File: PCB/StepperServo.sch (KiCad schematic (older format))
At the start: 69 parts, among them P1 Conn_01x06, P2 Conn_01x04, P4 Conn_01x08, P5 Conn_01x02, U1 BNOR11, U2 A4950E, U4 A4950E, U5 TLE5012B, U7 STM32F103CBTx, U8 LD1117S33CTR, U9 PCA82C251, Y1 Crystal, p7 Conn_01x08

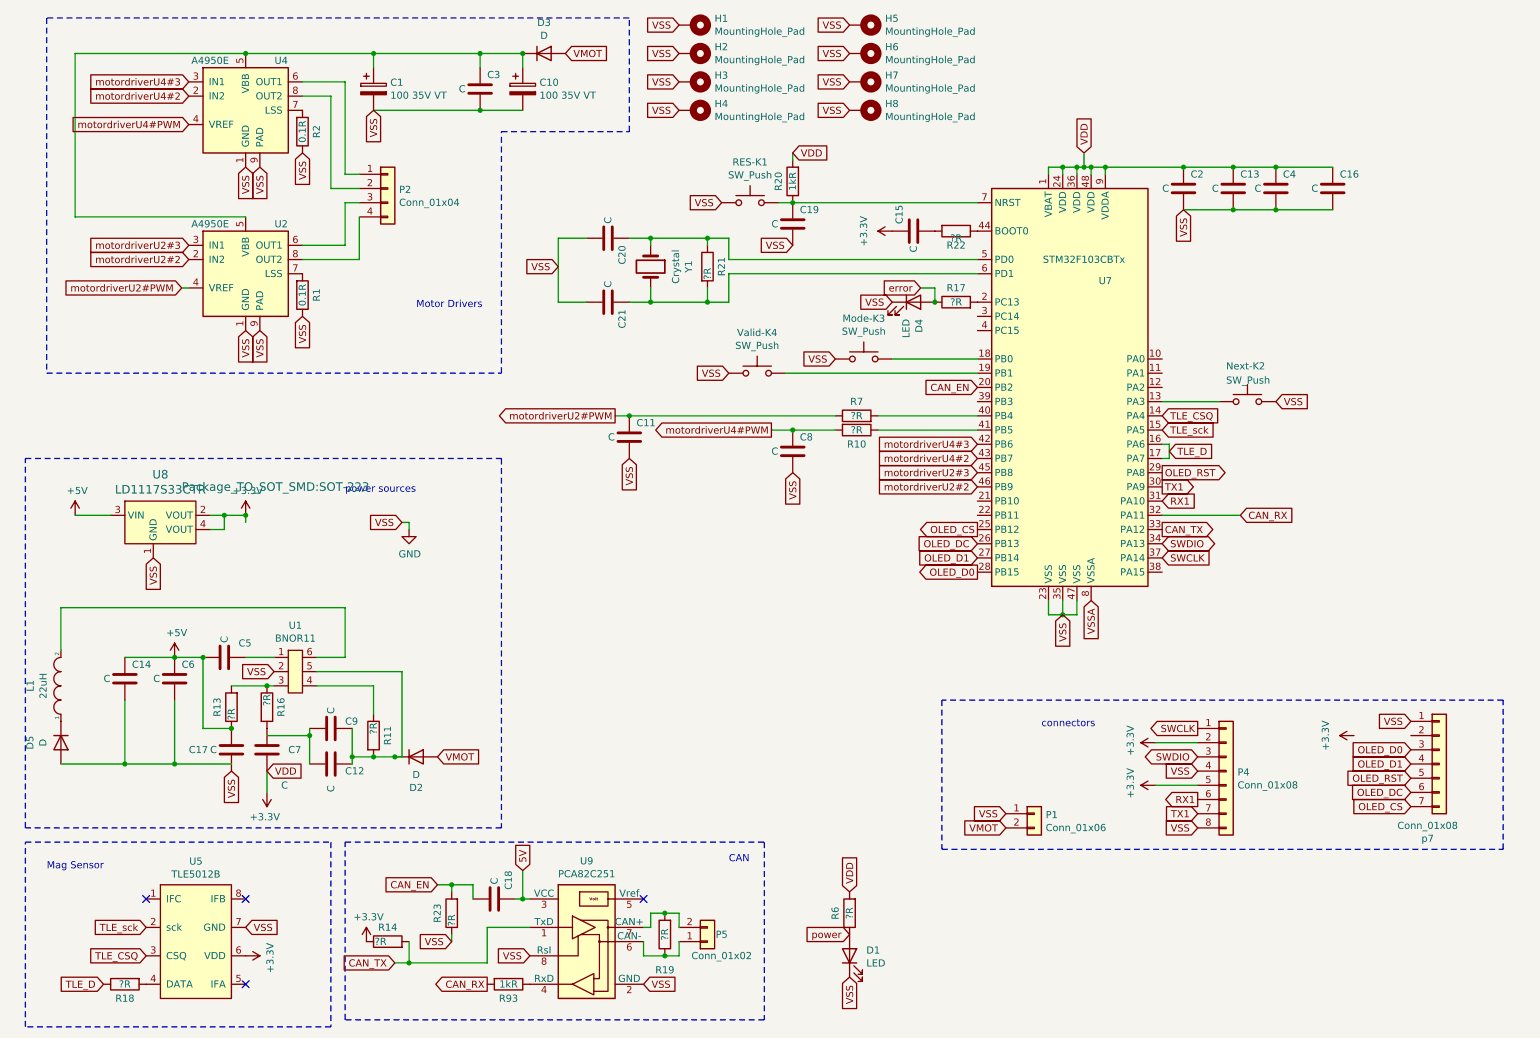
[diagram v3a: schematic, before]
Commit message: Boot0 to gnd
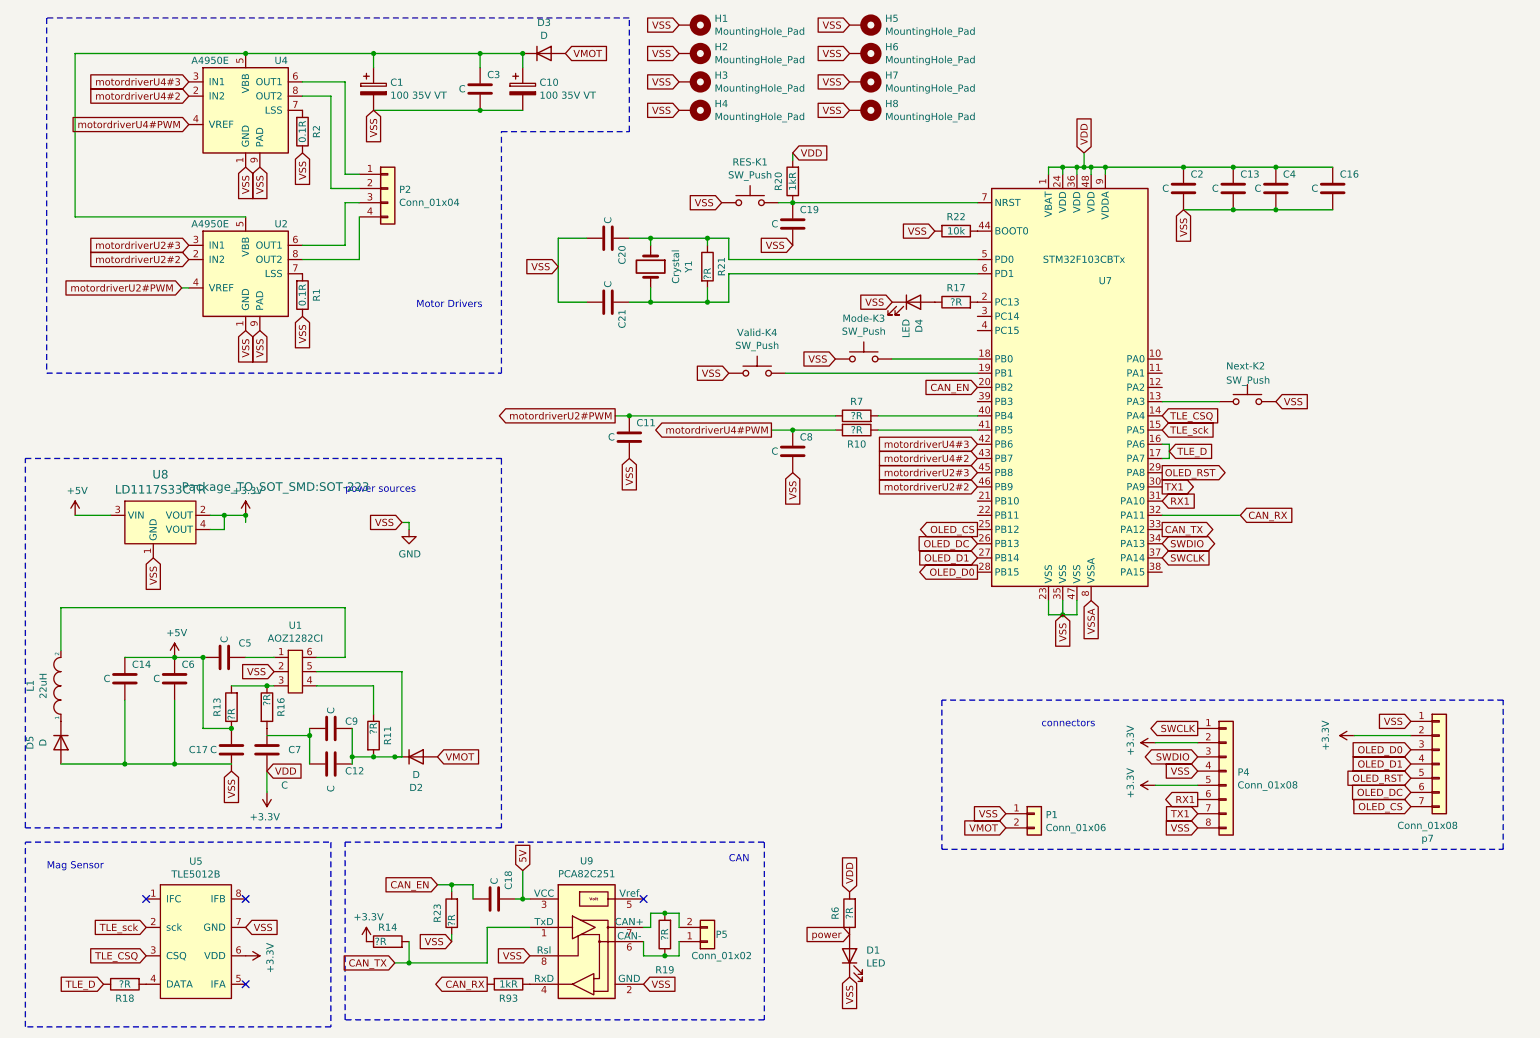
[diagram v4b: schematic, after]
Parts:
- removed C15: C, Capacitor_SMD:C_0603_1608Metric, symbol StepperServo-rescue:C-Device-BTTS57Bv2-rescue
- R22: value ?R -> 10k
- U1: value BNOR11 -> AOZ1282CI
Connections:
- net +3V3: now also p7.2 (Pin_2)
- net GND: now also R22.2
- net error: no longer names the net of D4.2 (A), R17.1
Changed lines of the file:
@@
-$EndComp
-$Comp
-L StepperServo-rescue:R-Device-BTTS57Bv2-rescue R17
-U 1 1 60AF1C31
-P 7150 2600
-F 0 "R17" V 7250 2600 50  0000 C CNN
-F 1 "?R" V 7150 2600 50  0000 C CNN
-F 2 "Resistor_SMD:R_0603_1608Metric" V 7080 2600 50  0001 C CNN
-F 3 "~" H 7150 2600 50  0001 C CNN
-	1    7150 2600
-	0    -1   -1   0
 $EndComp
 $Comp
@@
 Text GLabel 6400 7050 0    50   Input ~ 0
 power
-Text GLabel 6900 2500 0    50   Input ~ 0
-error
 Text GLabel 6700 2600 0    50   Input ~ 0
 VSS
@@
 	1    0    0    -1
 $EndComp
-Wire Wire Line
-	6900 2500 7000 2500
-Wire Wire Line
-	7000 2500 7000 2600
-Connection ~ 7000 2600
 $Comp
 L TLE5012B:TLE5012B U5
@@
 $EndComp
 $Comp
-L StepperServo-rescue:C-Device-BTTS57Bv2-rescue C15
-U 1 1 60B85066
-P 6850 2100
-F 0 "C15" H 6900 2200 50  0000 L CNN
-F 1 "C" H 6700 2100 50  0000 L CNN
-F 2 "Capacitor_SMD:C_0603_1608Metric" H 6888 1950 50  0001 C CNN
-F 3 "~" H 6850 2100 50  0001 C CNN
-	1    6850 2100
-	0    -1   -1   0
-$EndComp
-$Comp
 L StepperServo-rescue:R-Device-BTTS57Bv2-rescue R22
 U 1 1 60B85EFC
 P 7150 2100
-F 0 "R22" V 7250 2100 50  0000 C CNN
-F 1 "?R" V 7200 2100 50  0000 C CNN
+F 0 "R22" V 7050 2100 50  0000 C CNN
+F 1 "10k" V 7150 2100 50  0000 C CNN
 F 2 "Resistor_SMD:R_0603_1608Metric" V 7080 2100 50  0001 C CNN
 F 3 "~" H 7150 2100 50  0001 C CNN
@@
 P 2450 5450
 F 0 "U1" H 2500 6025 50  0000 C CNN
-F 1 "BNOR11" H 2500 5934 50  0000 C CNN
+F 1 "AOZ1282CI" H 2500 5934 50  0000 C CNN
 F 2 "Package_TO_SOT_SMD:SOT-23-6" H 2450 5450 50  0001 C CNN
 F 3 "" H 2450 5450 50  0001 C CNN
@@
 	3800 1250 4100 1250
 Connection ~ 3800 1250
-$Comp
-L StepperServo-rescue:+3.3V-power-BTTS57Bv2-rescue #PWR0109
-U 1 1 60F08C2A
-P 6700 2100
-F 0 "#PWR0109" H 6700 1950 50  0001 C CNN
-F 1 "+3.3V" H 6700 2300 50  0000 C CNN
-F 2 "" H 6700 2100 50  0001 C CNN
-F 3 "" H 6700 2100 50  0001 C CNN
-	1    6700 2100
-	0    -1   -1   0
-$EndComp
 Connection ~ 6000 1900
 Wire Wire Line
@@
 Wire Notes Line
 	2850 6400 5800 6400
+Wire Wire Line
+	9950 5650 10350 5650
+Text GLabel 7000 2100 0    50   Input ~ 0
+VSS
+$Comp
+L StepperServo-rescue:R-Device-BTTS57Bv2-rescue R17
+U 1 1 60AF1C31
+P 7150 2600
+F 0 "R17" V 7250 2600 50  0000 C CNN
+F 1 "?R" V 7150 2600 50  0000 C CNN
+F 2 "Resistor_SMD:R_0603_1608Metric" V 7080 2600 50  0001 C CNN
+F 3 "~" H 7150 2600 50  0001 C CNN
+	1    7150 2600
+	0    -1   -1   0
+$EndComp
 $EndSCHEMATC

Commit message: NRST pull'up most likely not needed - set to virtual. A bit of cleanup.
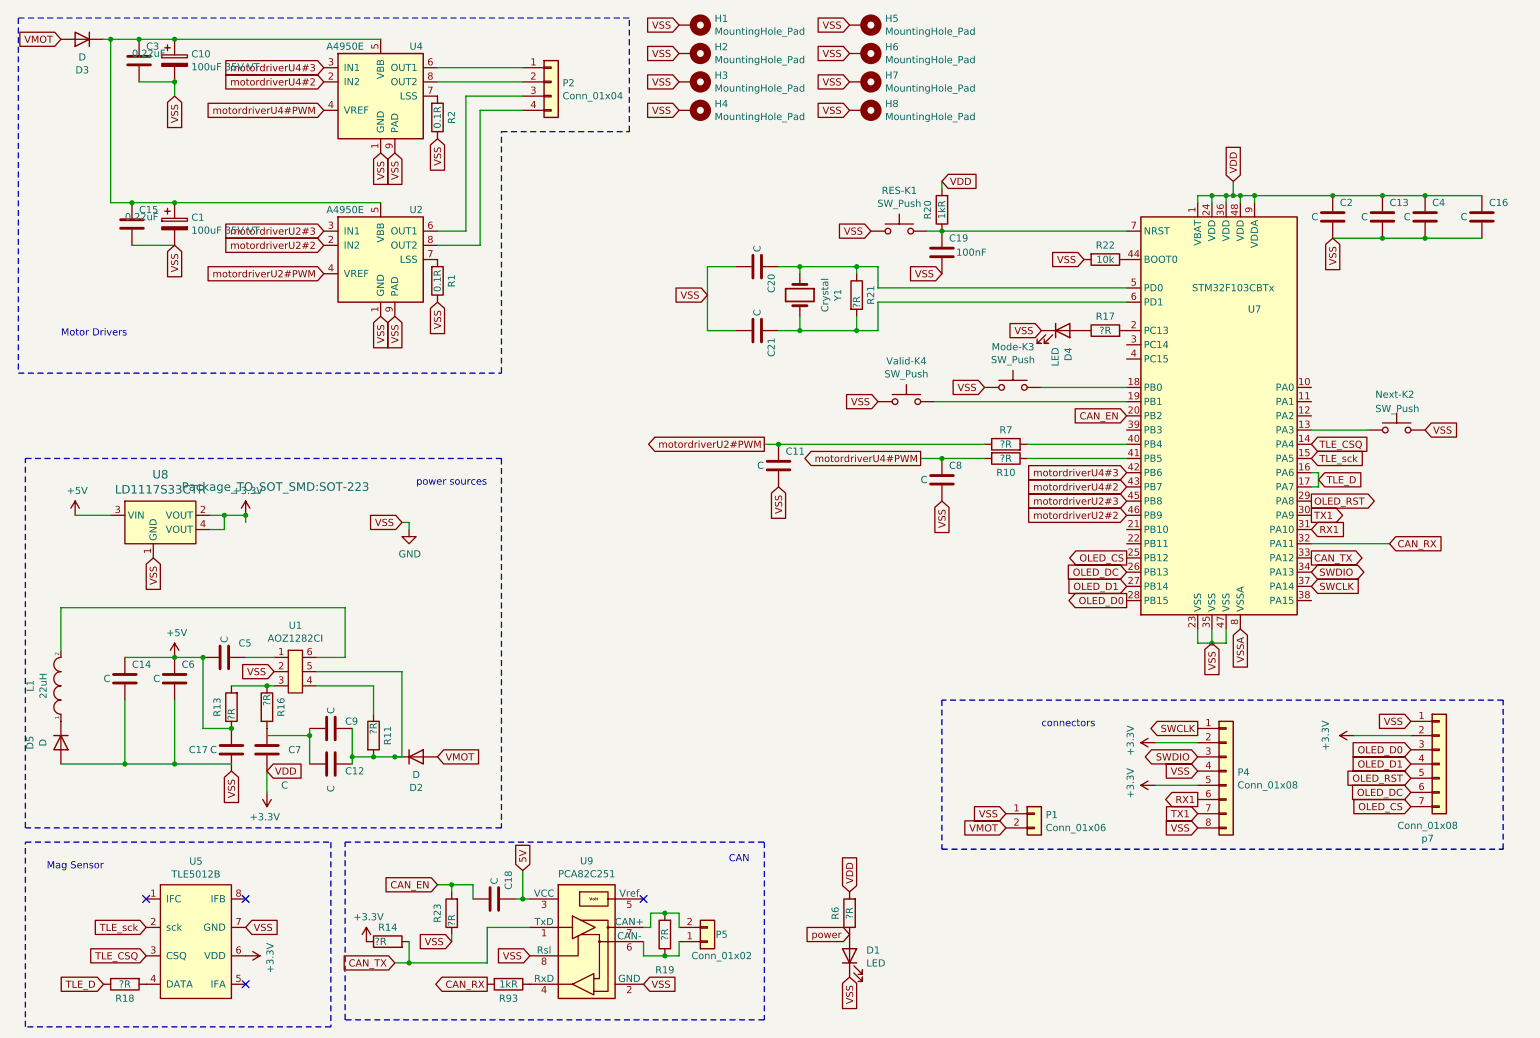
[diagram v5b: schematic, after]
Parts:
- added C15: 0.22uF, Capacitor_SMD:C_0805_2012Metric, symbol StepperServo-rescue:C-Device-BTTS57Bv2-rescue
- C1, C10: value 100 35V VT -> 100uF 35V VT
- C19: value C -> 100nF
- C3: value C -> 0.22uF
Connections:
- net GND: now also C15.2
- net at C1.1, C10.1, C3.1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: now also C15.1
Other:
- moved on the sheet: C1, C10, C11, C13, C16, C19, C2, C20, C21, C3, C4, C8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
